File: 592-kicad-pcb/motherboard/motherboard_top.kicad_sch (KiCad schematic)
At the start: 19 parts, among them J17 Conn_02x01, J18 Conn_02x01, J21 Conn_02x01, J22 Conn_02x01, U14 74CBTLV3257, U15 74CBTLV3257, U17 74CBTLV3257, U18 SN74LVC1G14DBV, U19 SN74LVC1G14DBV

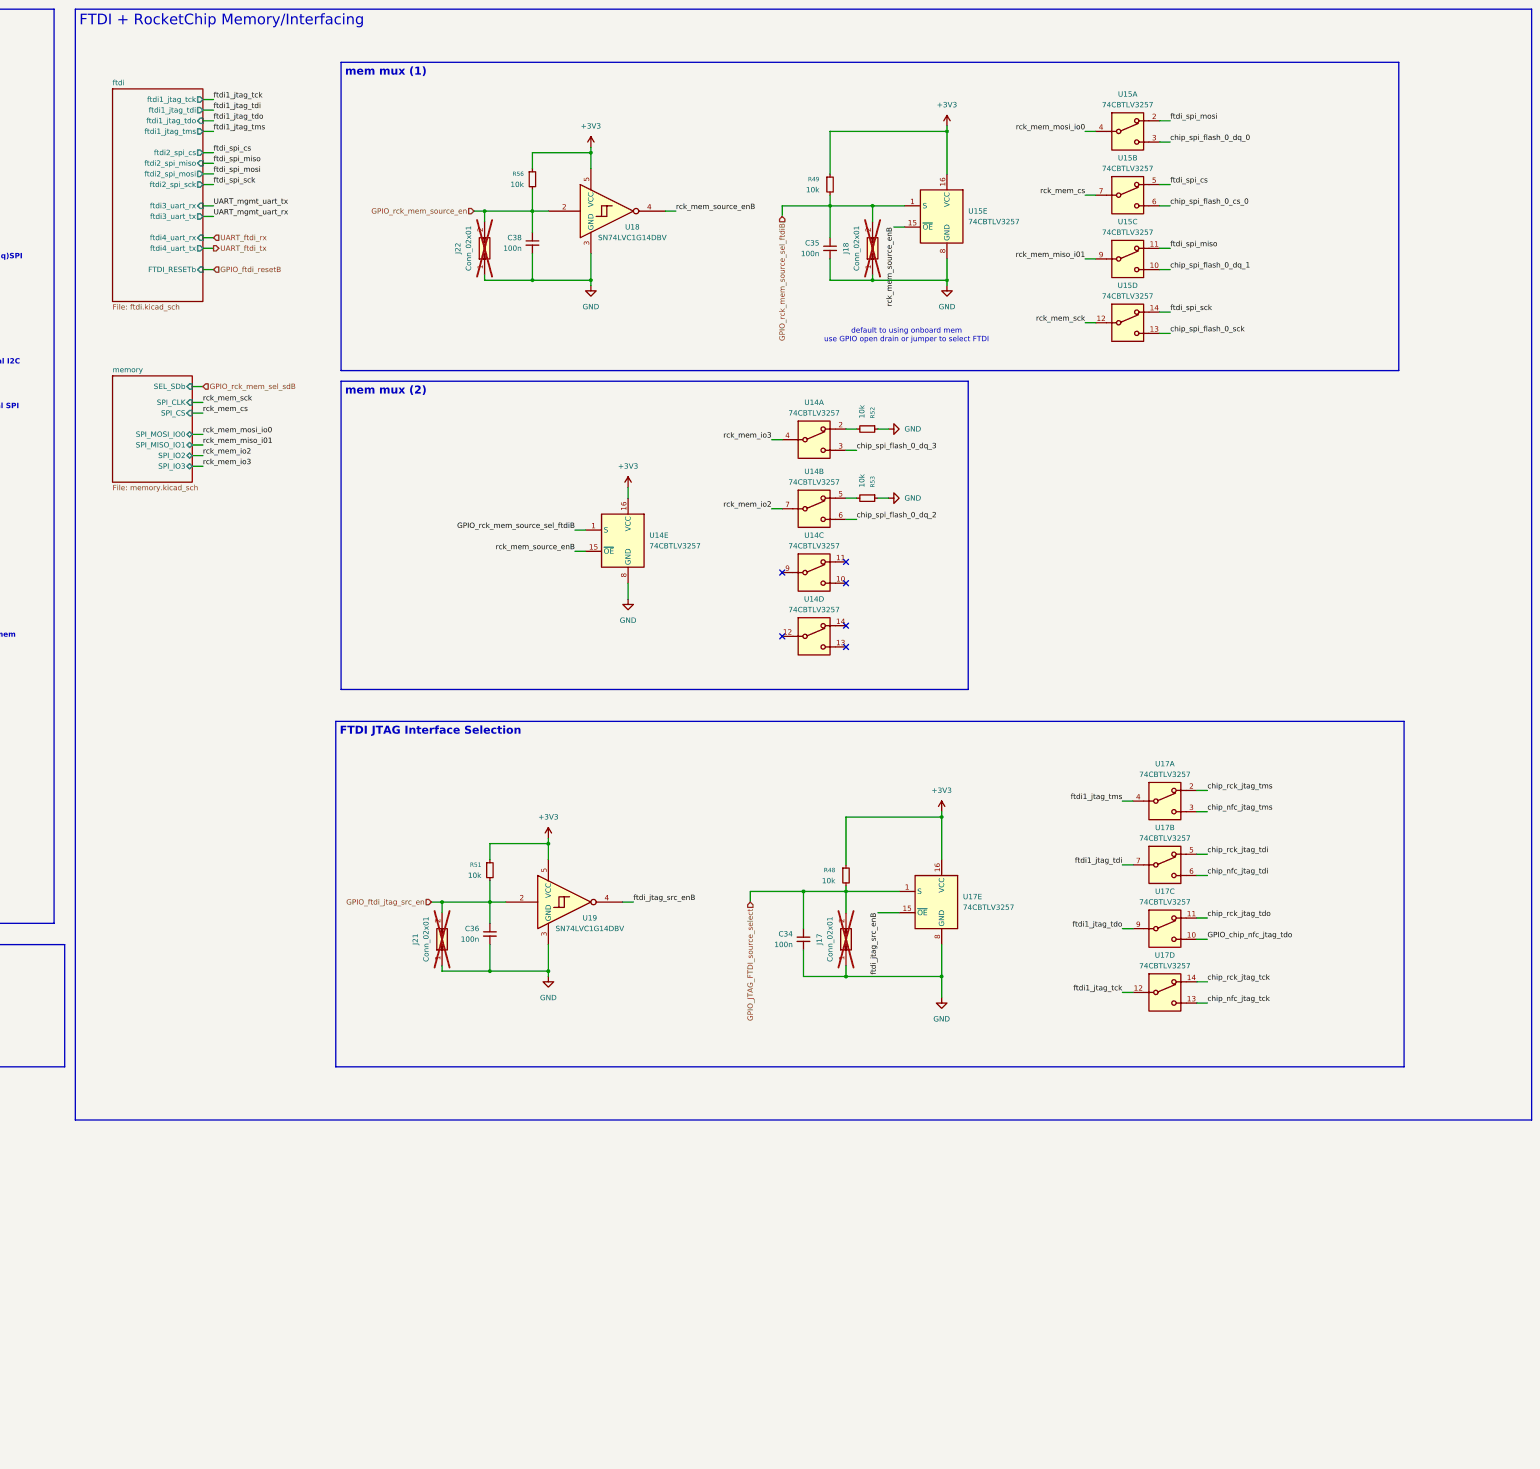
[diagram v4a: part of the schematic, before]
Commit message: add aux SPI dual-master to drive caravel CPU
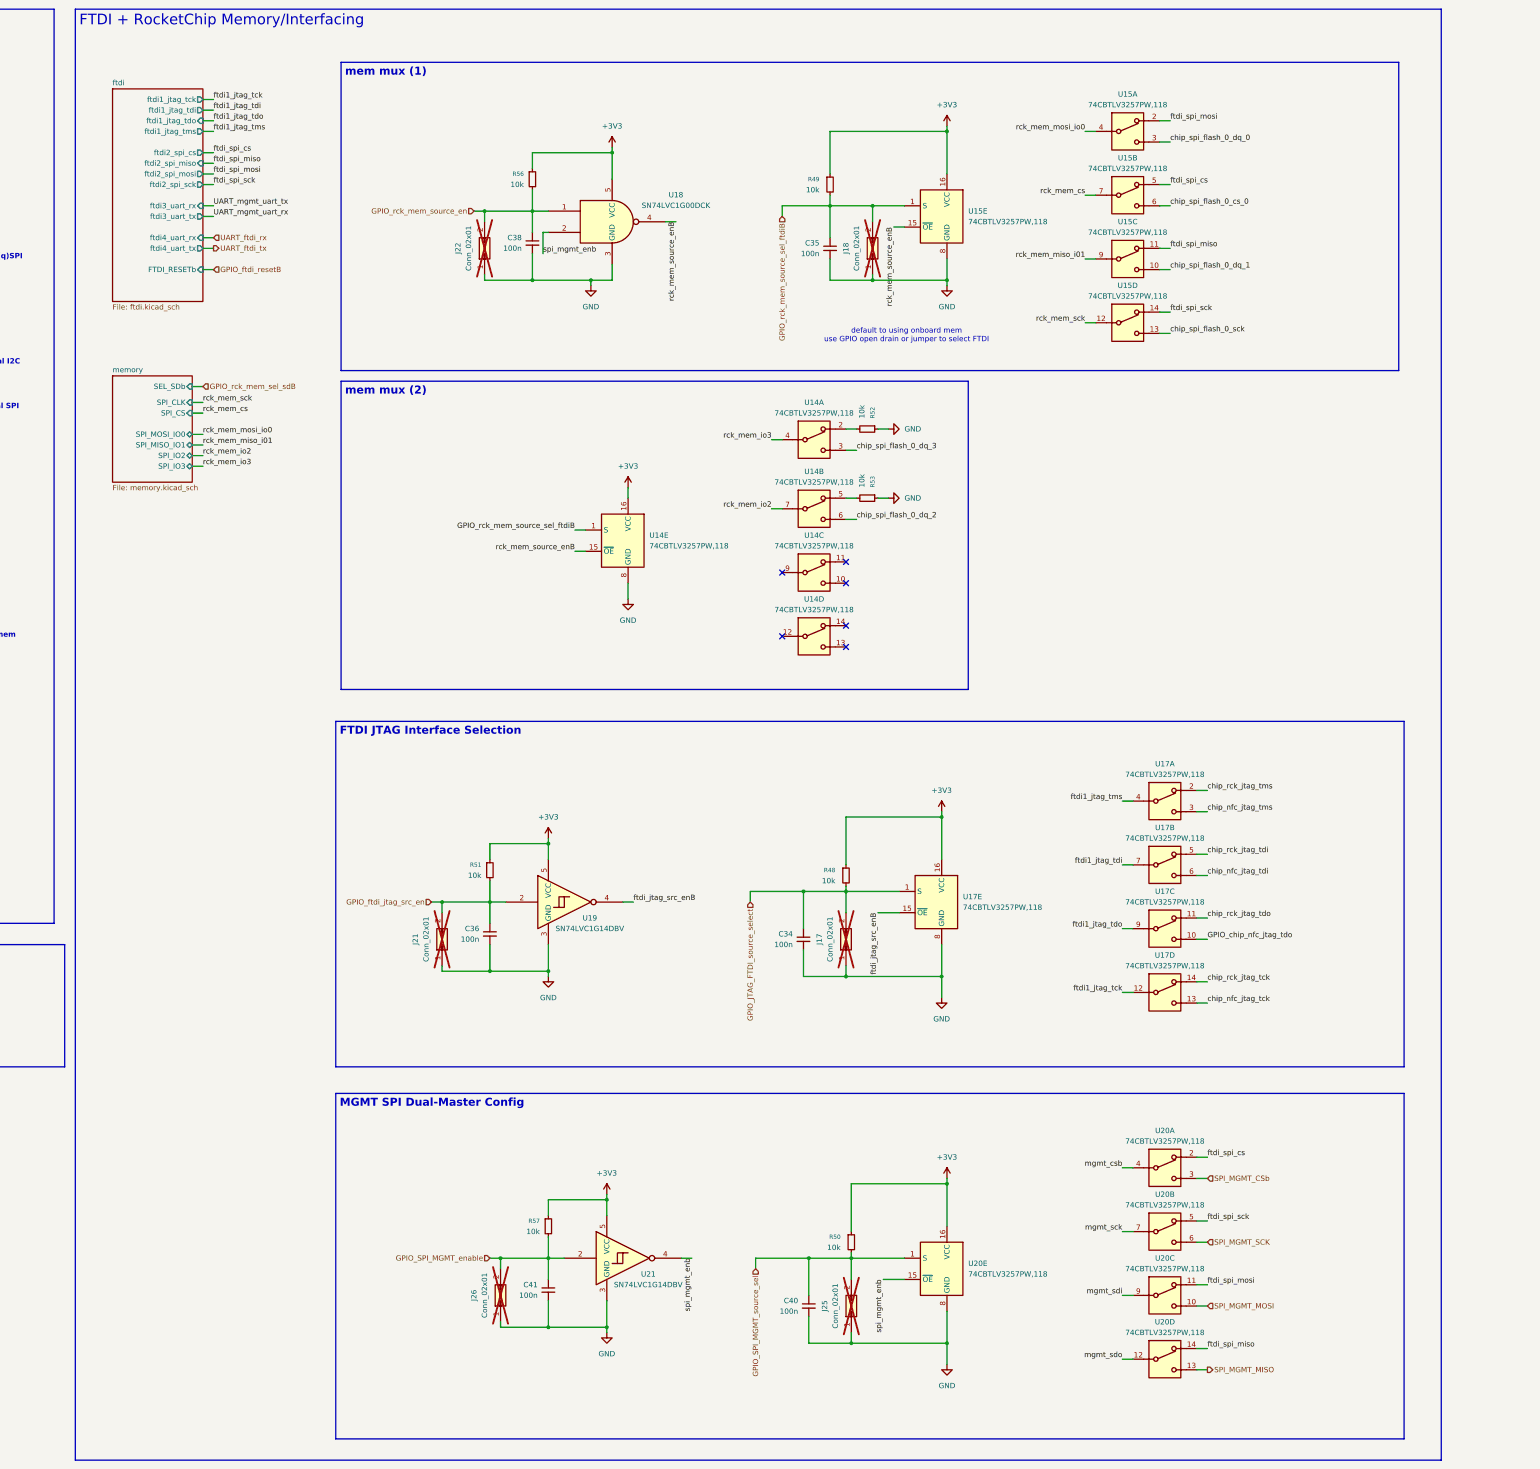
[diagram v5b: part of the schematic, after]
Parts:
- removed U18: SN74LVC1G14DBV, Package_TO_SOT_SMD:SOT-353_SC-70-5, symbol 74xGxx:SN74LVC1G14DBV
- added C40, C41: 100n, Capacitor_SMD:C_0402_1005Metric, symbol Device:C_Small
- added J25, J26: Conn_02x01, Connector_PinHeader_1.27mm:PinHeader_1x02_P1.27mm_Vertical, symbol Connector_Generic:Conn_02x01
- added R50, R57: 10k, Resistor_SMD:R_0402_1005Metric, symbol Device:R_Small
- added U18: SN74LVC1G00DCK, Package_TO_SOT_SMD:SOT-353_SC-70-5, symbol 74xGxx:SN74LVC1G00DCK
- added U20: 74CBTLV3257PW,118, Package_SO:TSSOP-16_4.4x5mm_P0.65mm, symbol 74xx:74CBTLV3257
- added U21: SN74LVC1G14DBV, Package_TO_SOT_SMD:SOT-353_SC-70-5, symbol 74xGxx:SN74LVC1G14DBV
- U14, U15, U17: value 74CBTLV3257 -> 74CBTLV3257PW,118; footprint Package_SO:SOIC-16_3.9x9.9mm_P1.27mm -> Package_SO:TSSOP-16_4.4x5mm_P0.65mm; LCSC C10012 -> C546455
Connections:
- net +3V3: now also R50.1, R57.1, U18.5 (VCC), U20.16 (VCC), U21.5 (VCC)
- net GND: now also C40.2, C41.2, J25.1 (Pin_1), J26.1 (Pin_1), U18.3 (GND), U20.8 (GND), U21.3 (GND)
- net GPIO_rck_mem_source_en: now also U18.1
- net ftdi_spi_cs: now also U20.2
- net ftdi_spi_miso: now also U20.14
- net ftdi_spi_mosi: now also U20.11
- net ftdi_spi_sck: now also U20.5
- net mgmt_csb: now also U20.4
- net mgmt_sck: now also U20.7
- net mgmt_sdi: now also U20.9
- net mgmt_sdo: now also U20.12
- net rck_mem_source_enB: now also U18.4
- new net GPIO_SPI_MGMT_enable: C41.1, J26.2 (Pin_2), R57.2, U21.2
- new net GPIO_SPI_MGMT_source_sel: C40.1, J25.2 (Pin_2), R50.2, U20.1 (S)
- new net SPI_MGMT_CSb: U20.3
- new net SPI_MGMT_MISO: U20.13
- new net SPI_MGMT_MOSI: U20.10
- new net SPI_MGMT_SCK: U20.6
- new net spi_mgmt_enb: U18.2, U20.15 (~{OE}), U21.4
